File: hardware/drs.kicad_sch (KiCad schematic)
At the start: 0 parts

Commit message: DRS-first commit
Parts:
- added C1: 10n, Capacitor_SMD:C_0603_1608Metric_Pad1.08x0.95mm_HandSolder, symbol Device:C_Small
- added J1: USB_C_Receptacle_USB2.0_14P, symbol Connector:USB_C_Receptacle_USB2.0_14P
- added J2: FTSH-107-01-L-DV-K-A, FTSH-107-XX-YYY-DV-K-A, symbol FTSH-107-01-L-DV-K-A:FTSH-107-01-L-DV-K-A
- added R2, R3: 5k1, symbol Device:R_Small
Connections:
- new net: J1.A5 (CC1), R2.1
- new net: J1.B5 (CC2), R3.2
- new net: C1.1, J1.S1 (SHIELD)
- new net +3.3V: J2.3
- new net GND: C1.2, J1.A1 (GND), J1.A12 (GND), J1.B1 (GND), J1.B12 (GND), J2.11, J2.5, J2.7, R2.2, R3.1
- new net RST: J2.12
- new net SWCLK: J2.6
- new net SWDIO: J2.4
- new net USART1_RX: J2.13
- new net USART1_TX: J2.14
- new net USB_D+: J1.A6 (D+), J1.B6 (D+)
- new net USB_D-: J1.A7 (D-), J1.B7 (D-)
- new net VBUS: J1.A4 (VBUS), J1.A9 (VBUS), J1.B4 (VBUS), J1.B9 (VBUS)
- no-connect marks 0 -> 5
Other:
- added sheet CAN (can.kicad_sch)
- added sheet Connectors (connectors.kicad_sch)
- added sheet Control (control.kicad_sch)
- added sheet Power (power.kicad_sch)
- added sheet Servo (servo.kicad_sch)
- note added: "CAN"
- note added: "Connectors"
- note added: "DRS"
- note added: "DRS-main"
- note added: "Programmer"
- note added: "USB-C connector"

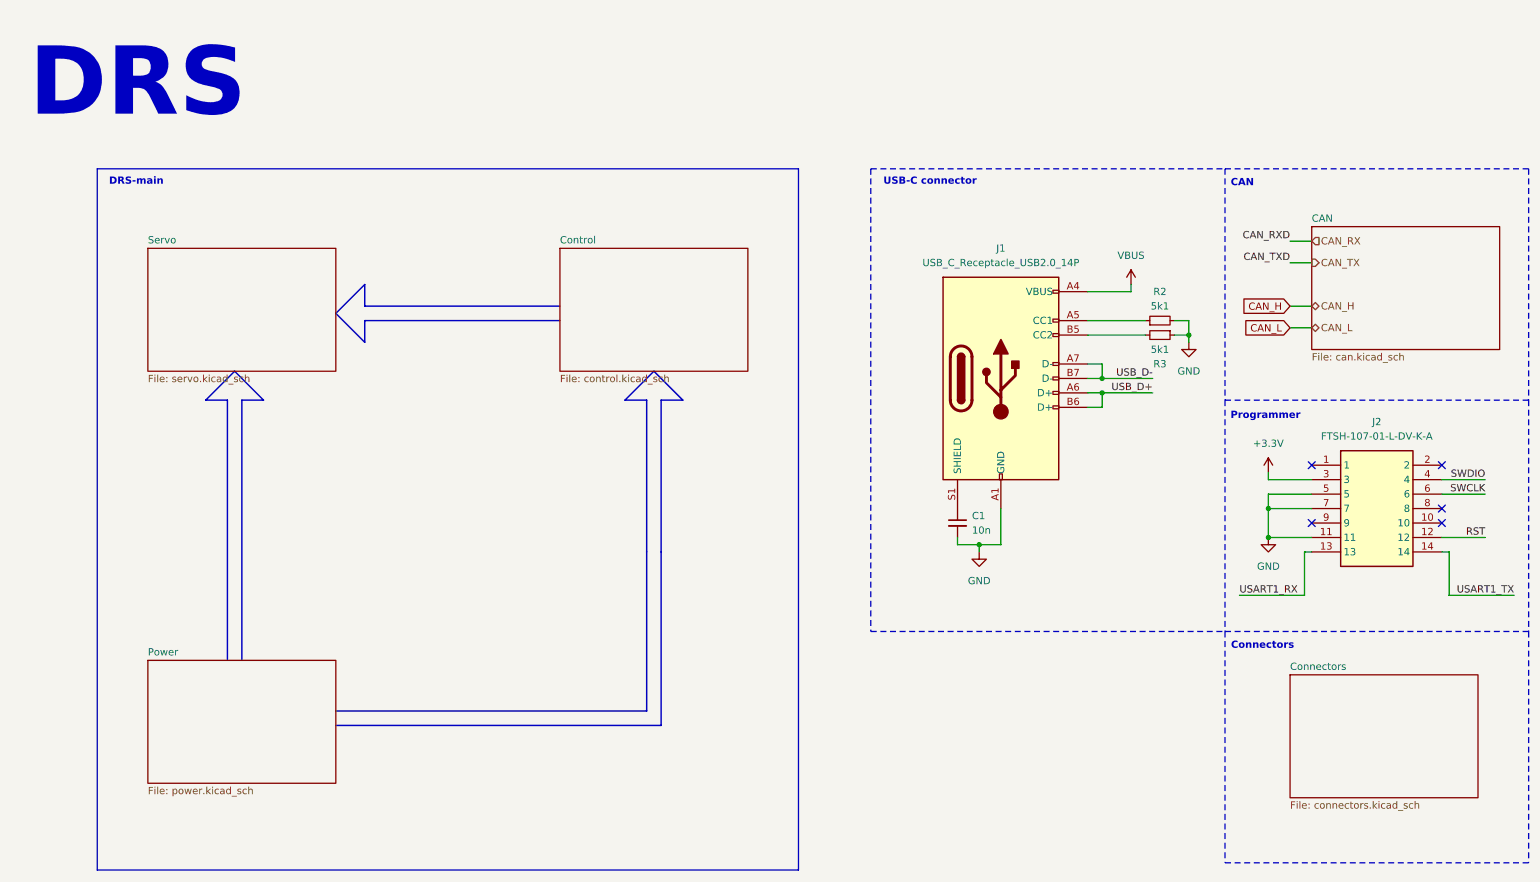
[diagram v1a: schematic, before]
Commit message: added sheet pins
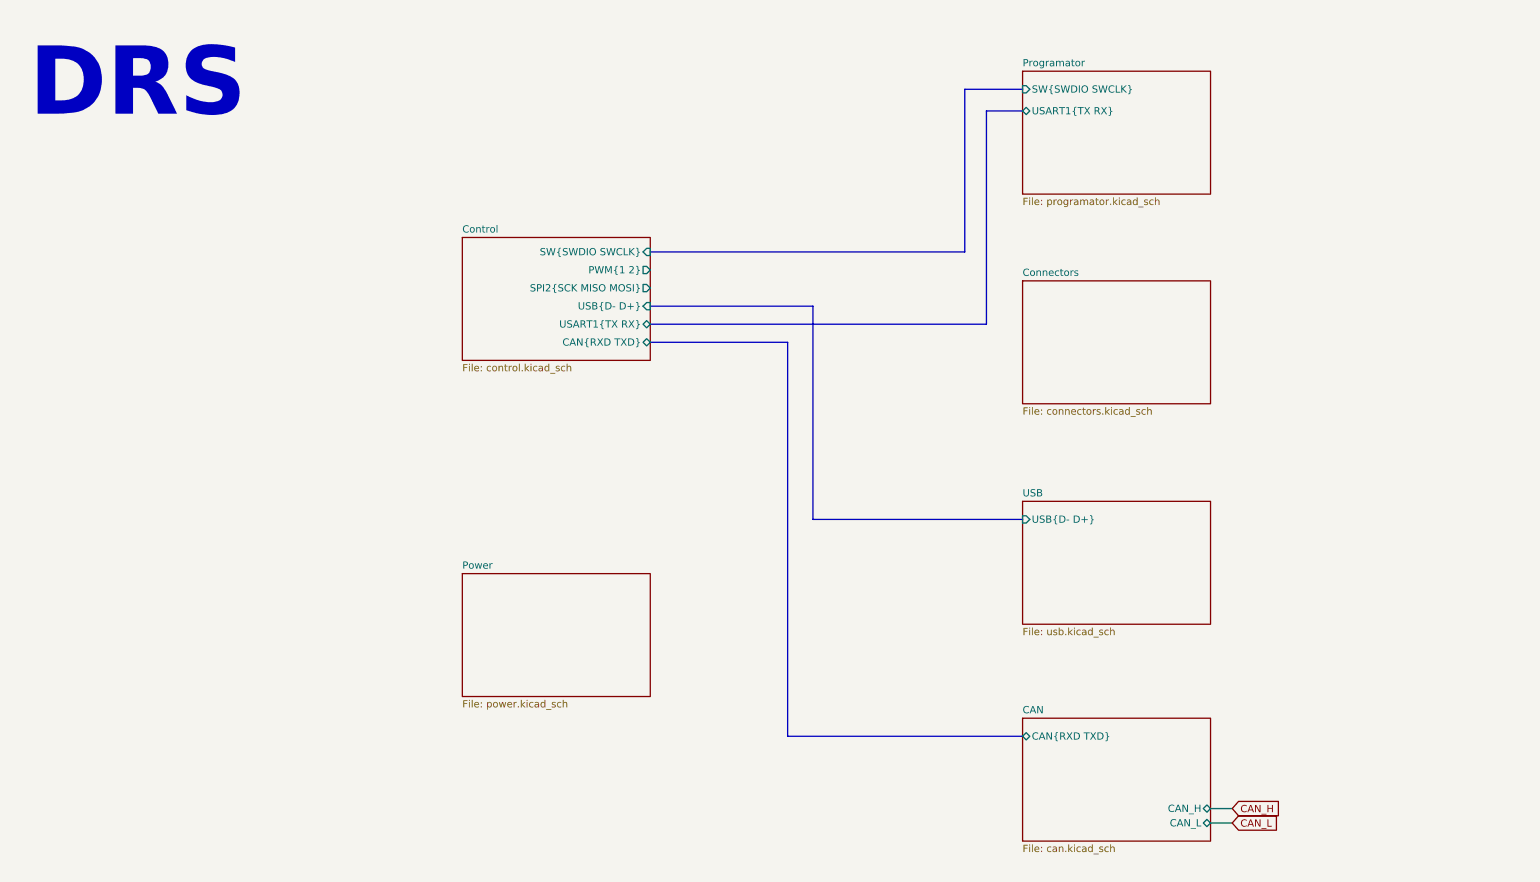
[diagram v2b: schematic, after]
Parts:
- removed C1: 10n, Capacitor_SMD:C_0603_1608Metric_Pad1.08x0.95mm_HandSolder, symbol Device:C_Small
- removed J1: USB_C_Receptacle_USB2.0_14P, symbol Connector:USB_C_Receptacle_USB2.0_14P
- removed J2: FTSH-107-01-L-DV-K-A, FTSH-107-XX-YYY-DV-K-A, symbol FTSH-107-01-L-DV-K-A:FTSH-107-01-L-DV-K-A
- removed R2, R3: 5k1, symbol Device:R_Small
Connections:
- no-connect marks 5 -> 0
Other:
- removed sheet Servo
- added sheet Programator (programator.kicad_sch)
- added sheet USB (usb.kicad_sch)
- sheet CAN ports: added CAN_H, CAN_L, CAN{RXD TXD}; removed none
- sheet Control ports: added CAN{RXD TXD}, PWM{1 2}, SPI2{SCK MISO MOSI}, SW{SWDIO SWCLK}, USART1{TX RX}, USB{D- D+}; removed none
- note removed: "CAN"
- note removed: "Connectors"
- note removed: "DRS-main"
- note removed: "Programmer"
- note removed: "USB-C connector"

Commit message: connectors - added, buses - todo
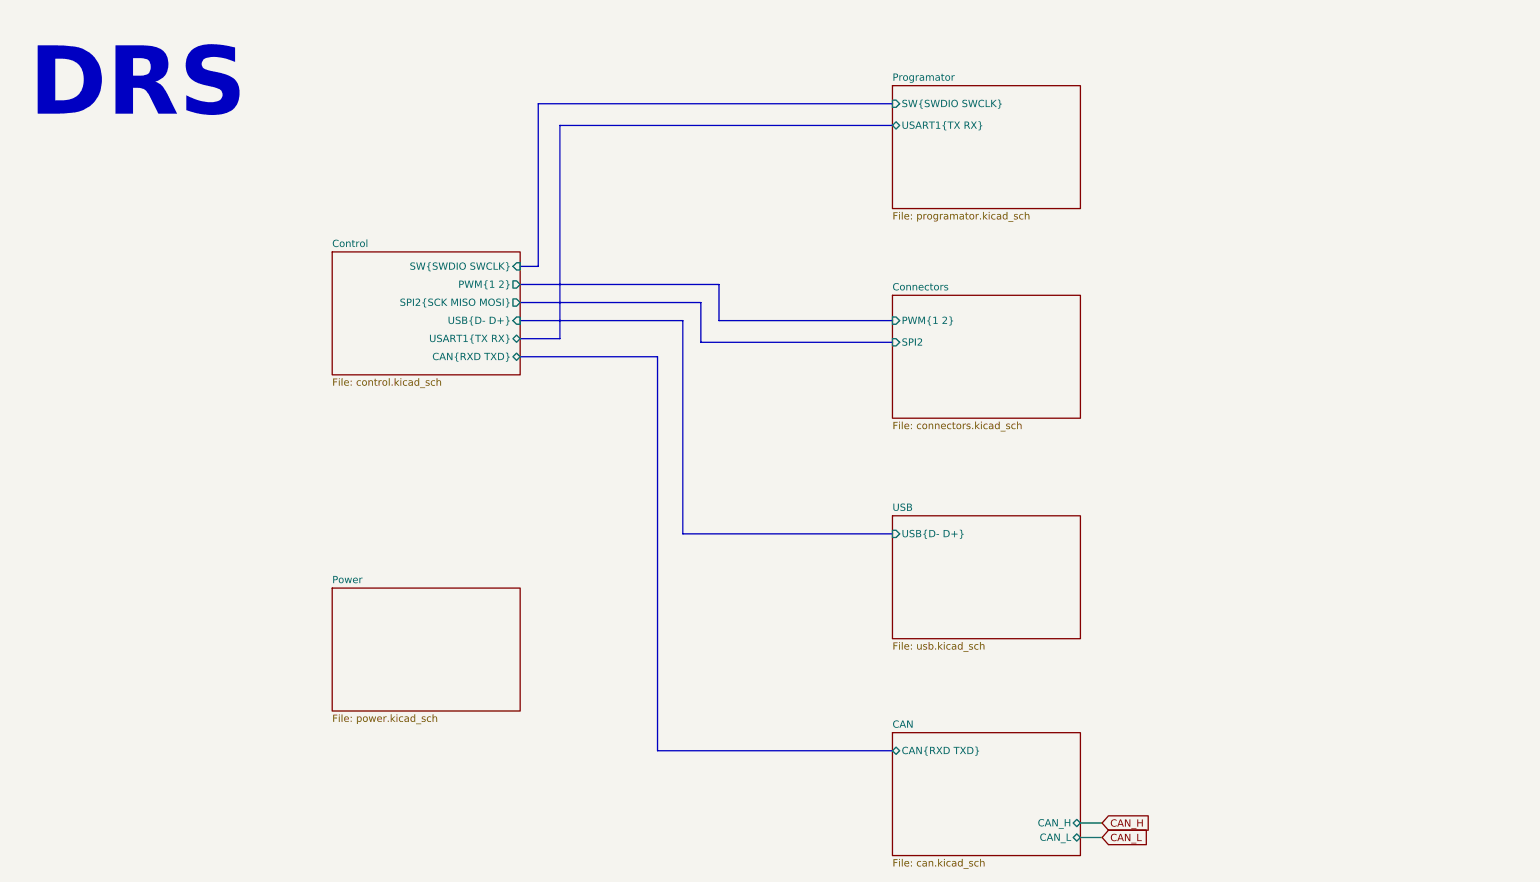
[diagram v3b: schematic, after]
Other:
- sheet Connectors ports: added PWM{1 2}, SPI2; removed none

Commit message: Poprawione busy, brak errorow
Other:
- removed sheet Programator
- removed sheet USB
- sheet CAN ports: added {CAN}; removed CAN{RXD TXD}
- sheet Connectors ports: added {PWM}, {SPI}, {SW}, {USART1}, {USB}; removed PWM{1 2}, SPI2
- sheet Control ports: added {CAN}, {PWM}, {SPI}, {SW}, {USART1}, {USB}; removed CAN{RXD TXD}, PWM{1 2}, SPI2{SCK MISO MOSI}, SW{SWDIO SWCLK}, USART1{TX RX}, USB{D- D+}

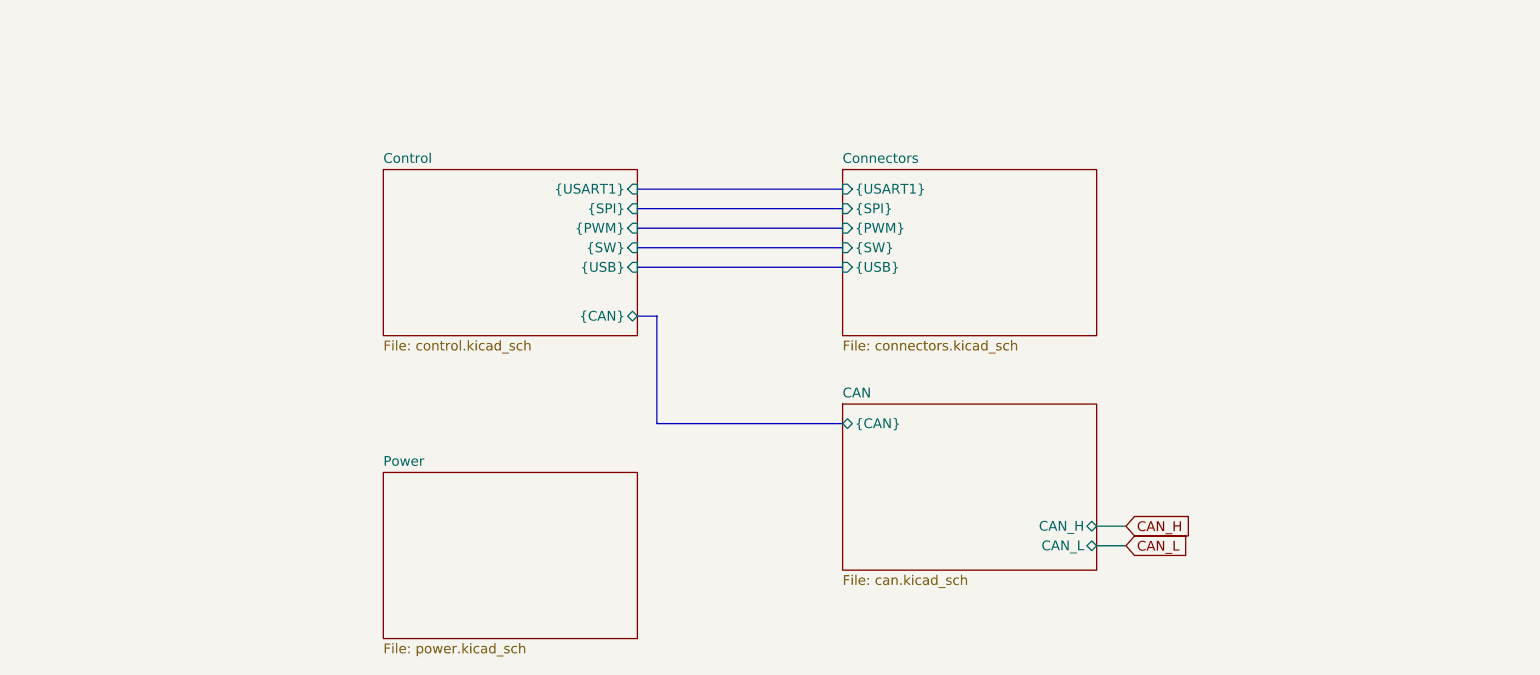
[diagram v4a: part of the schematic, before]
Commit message: Footprints addes beside PWM connectors
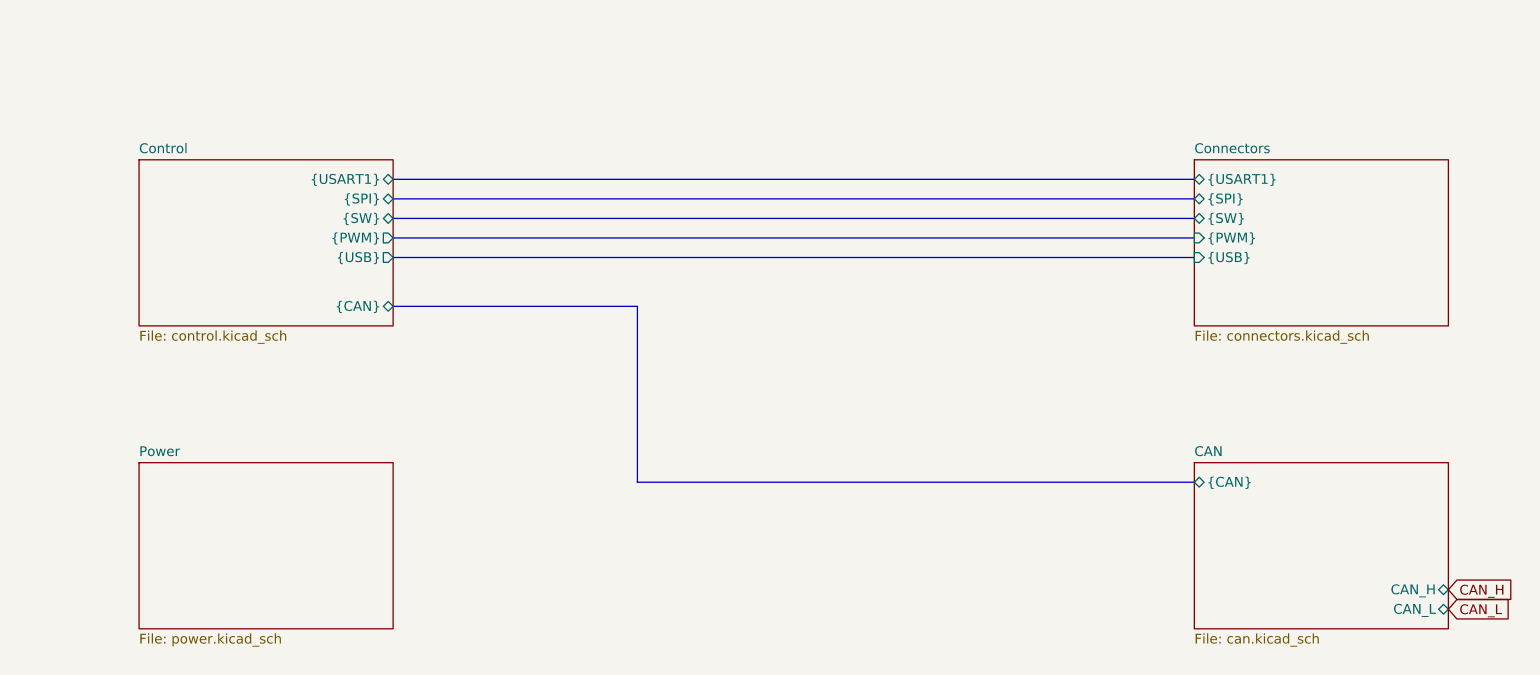
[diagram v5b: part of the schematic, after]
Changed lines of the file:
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@@
 	(bus
 		(pts
-			(xy 130.81 68.58) (xy 157.48 68.58)
-		)
-		(stroke
-			(width 0)
-			(type default)
-		)
-	)
-	(bus
-		(pts
-			(xy 130.81 73.66) (xy 157.48 73.66)
-		)
-		(stroke
-			(width 0)
-			(type default)
-		)
-	)
-	(bus
-		(pts
-			(xy 130.81 76.2) (xy 157.48 76.2)
-		)
-		(stroke
-			(width 0)
-			(type default)
-		)
-	)
-	(bus
-		(pts
-			(xy 130.81 85.09) (xy 133.35 85.09)
-		)
-		(stroke
-			(width 0)
-			(type default)
-		)
-	)
-	(wire
-		(pts
-			(xy 194.31 114.935) (xy 190.5 114.935)
-		)
-		(stroke
-			(width 0)
-			(type default)
-		)
-	)
-	(wire
-		(pts
-			(xy 194.31 112.395) (xy 190.5 112.395)
-		)
-		(stroke
-			(width 0)
-			(type default)
-		)
-	)
-	(bus
-		(pts
-			(xy 133.35 99.06) (xy 157.48 99.06)
-		)
-		(stroke
-			(width 0)
-			(type default)
-		)
-	)
-	(bus
-		(pts
-			(xy 130.81 71.12) (xy 157.48 71.12)
-		)
-		(stroke
-			(width 0)
-			(type default)
-		)
-	)
-	(bus
-		(pts
-			(xy 130.81 78.74) (xy 157.48 78.74)
-		)
-		(stroke
-			(width 0)
-			(type default)
-		)
-	)
-	(bus
-		(pts
-			(xy 133.35 85.09) (xy 133.35 99.06)
+			(xy 99.06 67.31) (xy 203.2 67.31)
+		)
+		(stroke
+			(width 0)
+			(type default)
+		)
+	)
+	(bus
+		(pts
+			(xy 99.06 83.82) (xy 130.81 83.82)
+		)
+		(stroke
+			(width 0)
+			(type default)
+		)
+	)
+	(bus
+		(pts
+			(xy 99.06 74.93) (xy 203.2 74.93)
+		)
+		(stroke
+			(width 0)
+			(type default)
+		)
+	)
+	(bus
+		(pts
+			(xy 130.81 106.68) (xy 203.2 106.68)
+		)
+		(stroke
+			(width 0)
+			(type default)
+		)
+	)
+	(bus
+		(pts
+			(xy 99.06 72.39) (xy 203.2 72.39)
+		)
+		(stroke
+			(width 0)
+			(type default)
+		)
+	)
+	(bus
+		(pts
+			(xy 99.06 69.85) (xy 203.2 69.85)
+		)
+		(stroke
+			(width 0)
+			(type default)
+		)
+	)
+	(bus
+		(pts
+			(xy 99.06 77.47) (xy 203.2 77.47)
+		)
+		(stroke
+			(width 0)
+			(type default)
+		)
+	)
+	(bus
+		(pts
+			(xy 130.81 83.82) (xy 130.81 106.68)
 		)
 		(stroke
@@
 	(global_label "CAN_H"
 		(shape input)
-		(at 194.31 112.395 0)
+		(at 236.22 120.65 0)
 		(fields_autoplaced yes)
 		(effects
@@
 		)
 		(property "Intersheetrefs" "${INTERSHEET_REFS}"
-			(at 203.2824 112.395 0)
+			(at 245.1924 120.65 0)
 			(effects
 				(font
@@
 	(global_label "CAN_L"
 		(shape input)
-		(at 194.31 114.935 0)
+		(at 236.22 123.19 0)
 		(fields_autoplaced yes)
 		(effects
@@
 		)
 		(property "Intersheetrefs" "${INTERSHEET_REFS}"
-			(at 202.98 114.935 0)
+			(at 244.89 123.19 0)
 			(effects
 				(font
@@
 	)
 	(sheet
-		(at 97.79 105.41)
+		(at 66.04 104.14)
 		(size 33.02 21.59)
 		(fields_autoplaced yes)
@@
 		)
 		(property "Sheetname" "Power"
-			(at 97.79 104.6984 0)
+			(at 66.04 103.4284 0)
 			(effects
 				(font
@@
 		)
 		(property "Sheetfile" "power.kicad_sch"
-			(at 97.79 127.5846 0)
+			(at 66.04 126.3146 0)
 			(effects
 				(font
@@
 	)
 	(sheet
-		(at 97.79 66.04)
+		(at 66.04 64.77)
 		(size 33.02 21.59)
 		(fields_autoplaced yes)
@@
 		)
 		(property "Sheetname" "Control"
-			(at 97.79 65.3284 0)
+			(at 66.04 64.0584 0)
 			(effects
 				(font
@@
 		)
 		(property "Sheetfile" "control.kicad_sch"
-			(at 97.79 88.2146 0)
+			(at 66.04 86.9446 0)
 			(effects
 				(font
@@
 			)
 		)
-		(pin "{USART1}" input
-			(at 130.81 68.58 0)
+		(pin "{USART1}" bidirectional
+			(at 99.06 67.31 0)
 			(effects
 				(font
@@
 		)
 		(pin "{CAN}" bidirectional
-			(at 130.81 85.09 0)
-			(effects
-				(font
-					(size 1.27 1.27)
-				)
-				(justify right)
-			)
-		)
-		(pin "{SPI}" input
-			(at 130.81 71.12 0)
-			(effects
-				(font
-					(size 1.27 1.27)
-				)
-				(justify right)
-			)
-		)
-		(pin "{PWM}" input
-			(at 130.81 73.66 0)
-			(effects
-				(font
-					(size 1.27 1.27)
-				)
-				(justify right)
-			)
-		)
-		(pin "{SW}" input
-			(at 130.81 76.2 0)
-			(effects
-				(font
-					(size 1.27 1.27)
-				)
-				(justify right)
-			)
-		)
-		(pin "{USB}" input
-			(at 130.81 78.74 0)
+			(at 99.06 83.82 0)
+			(effects
+				(font
+					(size 1.27 1.27)
+				)
+				(justify right)
+			)
+		)
+		(pin "{SPI}" bidirectional
+			(at 99.06 69.85 0)
+			(effects
+				(font
+					(size 1.27 1.27)
+				)
+				(justify right)
+			)
+		)
+		(pin "{PWM}" output
+			(at 99.06 74.93 0)
+			(effects
+				(font
+					(size 1.27 1.27)
+				)
+				(justify right)
+			)
+		)
+		(pin "{SW}" bidirectional
+			(at 99.06 72.39 0)
+			(effects
+				(font
+					(size 1.27 1.27)
+				)
+				(justify right)
+			)
+		)
+		(pin "{USB}" output
+			(at 99.06 77.47 0)
 			(effects
 				(font
@@
 	)
 	(sheet
-		(at 157.48 96.52)
+		(at 203.2 104.14)
 		(size 33.02 21.59)
 		(fields_autoplaced yes)
@@
 		)
 		(property "Sheetname" "CAN"
-			(at 157.48 95.8084 0)
+			(at 203.2 103.4284 0)
 			(effects
 				(font
@@
 		)
 		(property "Sheetfile" "can.kicad_sch"
-			(at 157.48 118.6946 0)
+			(at 203.2 126.3146 0)
 			(effects
 				(font
@@
 		)
 		(pin "CAN_H" bidirectional
-			(at 190.5 112.395 0)
+			(at 236.22 120.65 0)
 			(effects
 				(font
@@
 		)
 		(pin "CAN_L" bidirectional
-			(at 190.5 114.935 0)
+			(at 236.22 123.19 0)
 			(effects
 				(font
@@
 		)
 		(pin "{CAN}" bidirectional
-			(at 157.48 99.06 180)
+			(at 203.2 106.68 180)
 			(effects
 				(font
@@
 	)
 	(sheet
-		(at 157.48 66.04)
+		(at 203.2 64.77)
 		(size 33.02 21.59)
 		(fields_autoplaced yes)
@@
 		)
 		(property "Sheetname" "Connectors"
-			(at 157.48 65.3284 0)
+			(at 203.2 64.0584 0)
 			(effects
 				(font
@@
 		)
 		(property "Sheetfile" "connectors.kicad_sch"
-			(at 157.48 88.2146 0)
+			(at 203.2 86.9446 0)
 			(effects
 				(font
@@
 		)
 		(pin "{USB}" input
-			(at 157.48 78.74 180)
-			(effects
-				(font
-					(size 1.27 1.27)
-				)
-				(justify left)
-			)
-		)
-		(pin "{SPI}" input
-			(at 157.48 71.12 180)
+			(at 203.2 77.47 180)
+			(effects
+				(font
+					(size 1.27 1.27)
+				)
+				(justify left)
+			)
+		)
+		(pin "{SPI}" bidirectional
+			(at 203.2 69.85 180)
 			(effects
 				(font
@@
 		)
 		(pin "{PWM}" input
-			(at 157.48 73.66 180)
-			(effects
-				(font
-					(size 1.27 1.27)
-				)
-				(justify left)
-			)
-		)
-		(pin "{USART1}" input
-			(at 157.48 68.58 180)
-			(effects
-				(font
-					(size 1.27 1.27)
-				)
-				(justify left)
-			)
-		)
-		(pin "{SW}" input
-			(at 157.48 76.2 180)
-			(effects
-				(font
+			(at 203.2 74.93 180)
+			(effects
+				(font
+					(size 1.27 1.27)
+				)
+				(justify left)
+			)
+		)
+		(pin "{USART1}" bidirectional
+			(at 203.2 67.31 180)
+			(effects
+				(font
+					(size 1.27 1.27)
+				)
+				(justify left)
+			)
+		)
+		(pin "{SW}" bidirectional
+			(at 203.2 72.39 180)
+			(effects
+				(font
